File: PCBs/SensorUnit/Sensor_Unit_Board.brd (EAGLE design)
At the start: 68.6 x 39 mm, 7 parts

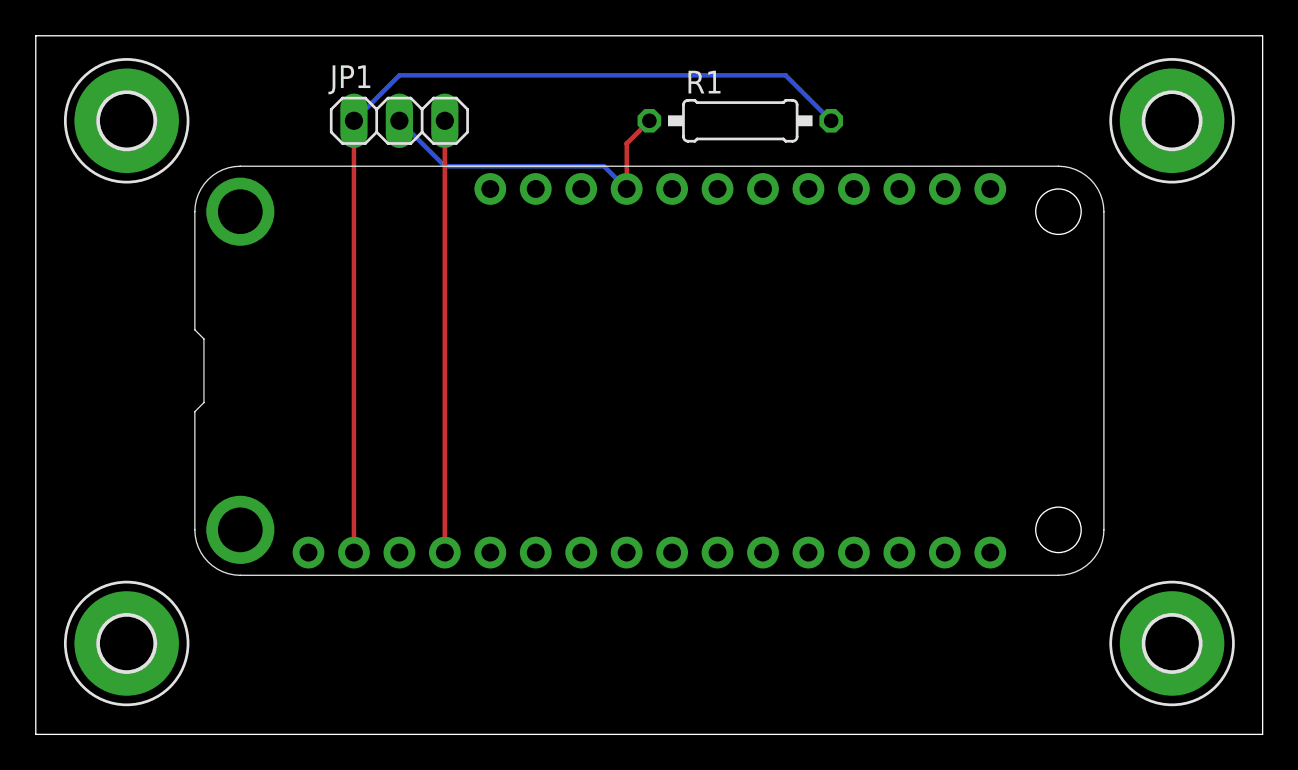
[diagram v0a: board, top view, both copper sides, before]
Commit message: Control Unit PCB finished, Sensor unit almost
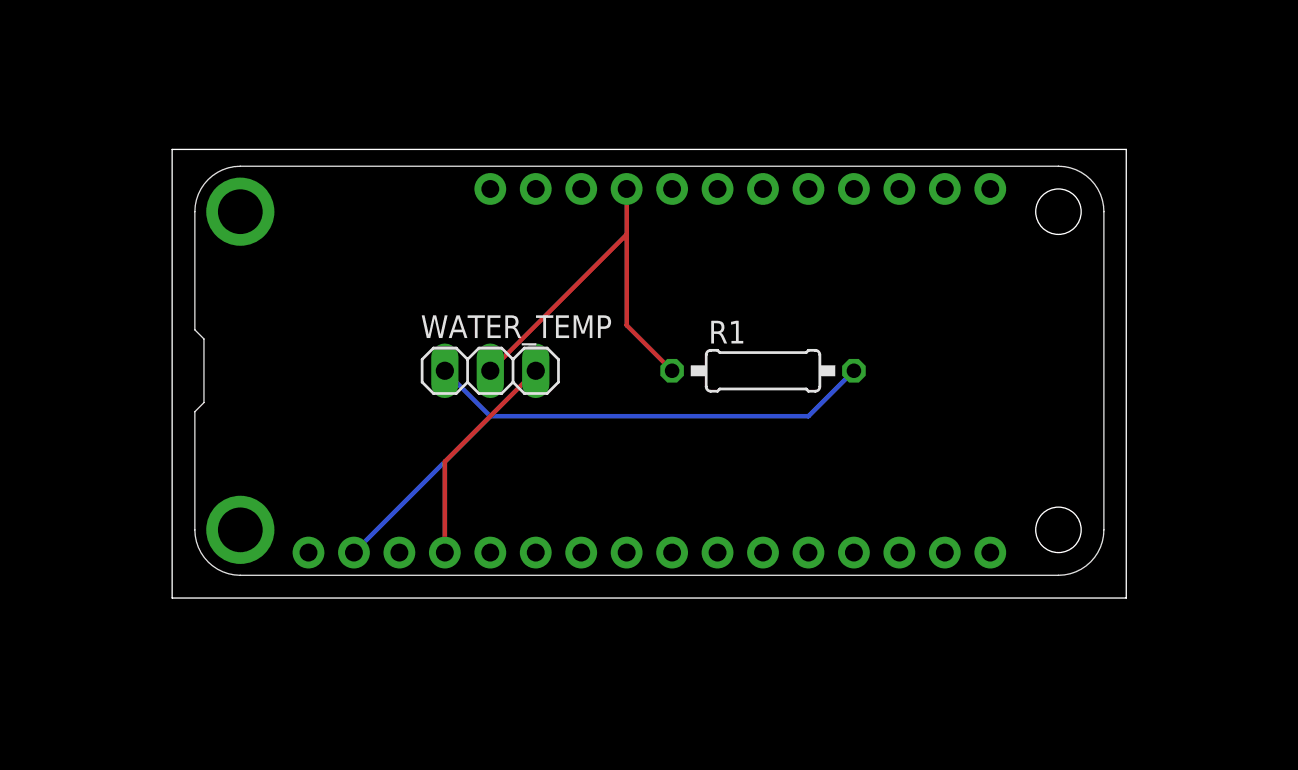
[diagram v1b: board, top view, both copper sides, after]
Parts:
- removed E$1, E$2, E$3, E$4: (no value), holes:3,0-PAD
- removed JP1: (no value), pinhead:1X03
- added WATER_TEMP: (no value), pinhead:1X03
- moved R1 14.0 mm to (40.6, 81.3)
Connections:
- net GND: now also WATER_TEMP.3; no longer JP1.3
- net N$4: now also WATER_TEMP.2; no longer JP1.2
- net VCC: now also WATER_TEMP.1; no longer JP1.1
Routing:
- net VCC: track 52.9 -> 35.7 mm
- net GND: track 24.1 -> 12.3 mm
- net N$4: track 18.6 -> 22.0 mm
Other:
- board size 68.6 x 39 mm -> 53.3 x 25.1 mm
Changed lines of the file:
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@@
 <board>
 <plain>
-<wire x1="0" y1="60.96" x2="68.56" y2="60.96" width="0" layer="20"/>
-<wire x1="68.56" y1="60.96" x2="68.56" y2="100" width="0" layer="20"/>
-<wire x1="68.56" y1="100" x2="0" y2="100" width="0" layer="20"/>
-<wire x1="0" y1="100" x2="0" y2="60.96" width="0" layer="20"/>
+<wire x1="7.62" y1="68.58" x2="60.94" y2="68.58" width="0" layer="20"/>
+<wire x1="60.94" y1="68.58" x2="60.94" y2="93.65" width="0" layer="20"/>
+<wire x1="60.94" y1="93.65" x2="7.62" y2="93.65" width="0" layer="20"/>
+<wire x1="7.62" y1="93.65" x2="7.62" y2="68.58" width="0" layer="20"/>
 </plain>
 <attributes>
@@
 <elements>
 <element name="MS1" library="adafruit" package="FEATHERWING_DIM" value="FEATHERWING_NODIM" x="8.89" y="69.85"/>
-<element name="R1" library="rcl" package="0207/10" value="" x="39.37" y="95.25"/>
-<element name="JP1" library="pinhead" package="1X03" value="" x="20.32" y="95.25"/>
-<element name="E$1" library="holes" package="3,0-PAD" value="" x="63.5" y="95.25"/>
-<element name="E$2" library="holes" package="3,0-PAD" value="" x="5.08" y="95.25"/>
-<element name="E$3" library="holes" package="3,0-PAD" value="" x="5.08" y="66.04"/>
-<element name="E$4" library="holes" package="3,0-PAD" value="" x="63.5" y="66.04"/>
+<element name="R1" library="rcl" package="0207/10" value="" x="40.64" y="81.28"/>
+<element name="WATER_TEMP" library="pinhead" package="1X03" value="" x="25.4" y="81.28"/>
 </elements>
 <signals>
 <signal name="GND">
 <contactref element="MS1" pad="4"/>
-<contactref element="JP1" pad="3"/>
-<wire x1="22.86" y1="71.12" x2="22.86" y2="95.25" width="0.254" layer="1"/>
+<contactref element="WATER_TEMP" pad="3"/>
+<wire x1="22.86" y1="76.2" x2="27.94" y2="81.28" width="0.254" layer="1"/>
+<wire x1="22.86" y1="71.12" x2="22.86" y2="76.2" width="0.254" layer="1"/>
 </signal>
 <signal name="VCC">
 <contactref element="MS1" pad="2"/>
-<contactref element="JP1" pad="1"/>
+<contactref element="WATER_TEMP" pad="1"/>
 <contactref element="R1" pad="2"/>
-<wire x1="41.91" y1="97.79" x2="44.45" y2="95.25" width="0.254" layer="16"/>
-<wire x1="20.32" y1="97.79" x2="41.91" y2="97.79" width="0.254" layer="16"/>
-<wire x1="17.78" y1="95.25" x2="20.32" y2="97.79" width="0.254" layer="16"/>
-<wire x1="17.78" y1="95.25" x2="17.78" y2="71.12" width="0.254" layer="1"/>
+<wire x1="43.18" y1="78.74" x2="45.72" y2="81.28" width="0.254" layer="16"/>
+<wire x1="25.4" y1="78.74" x2="43.18" y2="78.74" width="0.254" layer="16"/>
+<wire x1="22.86" y1="81.28" x2="25.4" y2="78.74" width="0.254" layer="16"/>
+<wire x1="25.4" y1="78.74" x2="17.78" y2="71.12" width="0.254" layer="16"/>
 </signal>
 <signal name="N$4">
-<contactref element="JP1" pad="2"/>
+<contactref element="WATER_TEMP" pad="2"/>
 <contactref element="R1" pad="1"/>
 <contactref element="MS1" pad="25"/>
-<wire x1="33.02" y1="93.98" x2="34.29" y2="95.25" width="0.254" layer="1"/>
-<wire x1="33.02" y1="91.44" x2="33.02" y2="93.98" width="0.254" layer="1"/>
-<wire x1="22.86" y1="92.71" x2="20.32" y2="95.25" width="0.254" layer="16"/>
-<wire x1="31.75" y1="92.71" x2="22.86" y2="92.71" width="0.254" layer="16"/>
-<wire x1="33.02" y1="91.44" x2="31.75" y2="92.71" width="0.254" layer="16"/>
+<wire x1="33.02" y1="83.82" x2="35.56" y2="81.28" width="0.254" layer="1"/>
+<wire x1="33.02" y1="91.44" x2="33.02" y2="88.9" width="0.254" layer="1"/>
+<wire x1="33.02" y1="88.9" x2="33.02" y2="83.82" width="0.254" layer="1"/>
+<wire x1="33.02" y1="88.9" x2="25.4" y2="81.28" width="0.254" layer="1"/>
 </signal>
 </signals>
